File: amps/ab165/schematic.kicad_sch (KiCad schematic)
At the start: 105 parts

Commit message: Fix: schematic sheets — real title block, fitted paper, no lettering through circuitry
Every sheet in the corpus shipped with an EMPTY title block ("Title:" and
"Date:" blank, default "Sheet /" furniture) laid onto a fixed A4/A3 page
regardless of the drawing's size, with prose annotations placed by hand
wherever a coordinate looked free when the amp was first drawn. The result
read as an unfinished alpha under a `verified` badge: KiCanvas's default view
is `zoom_to_page()`, so a 150 x 110 mm circuit on an A3 sheet opened as a
postage stamp, and later edits had pushed live circuitry under the prose.

schematic_lib.py — the builder now records each element as a (kind, points,
extra) tuple instead of a finished string, so `write()` can measure and move
what it emits:

- emits a real `(title_block …)` read from the amp's own meta.yaml — Title =
  designation + style, Date = the verification (or added) date, Rev = the
  verification status, Company = Circuit Codex, plus the licence and source
  URL as comments. Fixes all 34 sheets from one place;
- emits `(paper "User" w h)` cut to the drawing, translated to a fixed margin,
  with the bottom 34 mm strip reserved for the worksheet's title block. Sheet
  utilisation of the drawable area went from as low as ~20% to 92-98%;
- `note()` queues prose into a wrapped band under the circuit, and `caption()`
  places a section heading over the block it names, nudging it clear if it
  would print through anything;
- per-symbol default label offsets (the old single default printed every pot's
  value through its own wiper arrow and every transformer's designator through
  its body), plus `place_labels()`, which moves any designator/value block that
  would print over ink;
- transformers and chokes are drawn, not boxed: iron core between two windings,
  centre taps where the part has them, and an optional `spec` lettering slot for
  a ratio or impedance;
- `gnd()` takes a direction, because a flag defaulting to "down" at the HEAD of
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
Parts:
- V1A, V1B, V2A, V2B, V3B: value 12AX7 -> 12AX7 (7025)
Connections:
- net at CBB.1, CBB2.1, CDEEP.1: no longer RSB.2
- net at CBN.1, CBN2.1: no longer RSN.2
- net at CTN.2: no longer VRTN.1
- net at DBIAS.2 (K): no longer RBIAS.2
- net at CTB.2: no longer VRTB.1
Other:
- note removed: "AB165 — Blackface Bassman-style · Circuit Codex · CC-BY-SA 4.0 · redrawn from circuit facts"
- company: (none) -> Circuit Codex
- title: (none) -> AB165 — Blackface Bassman-style

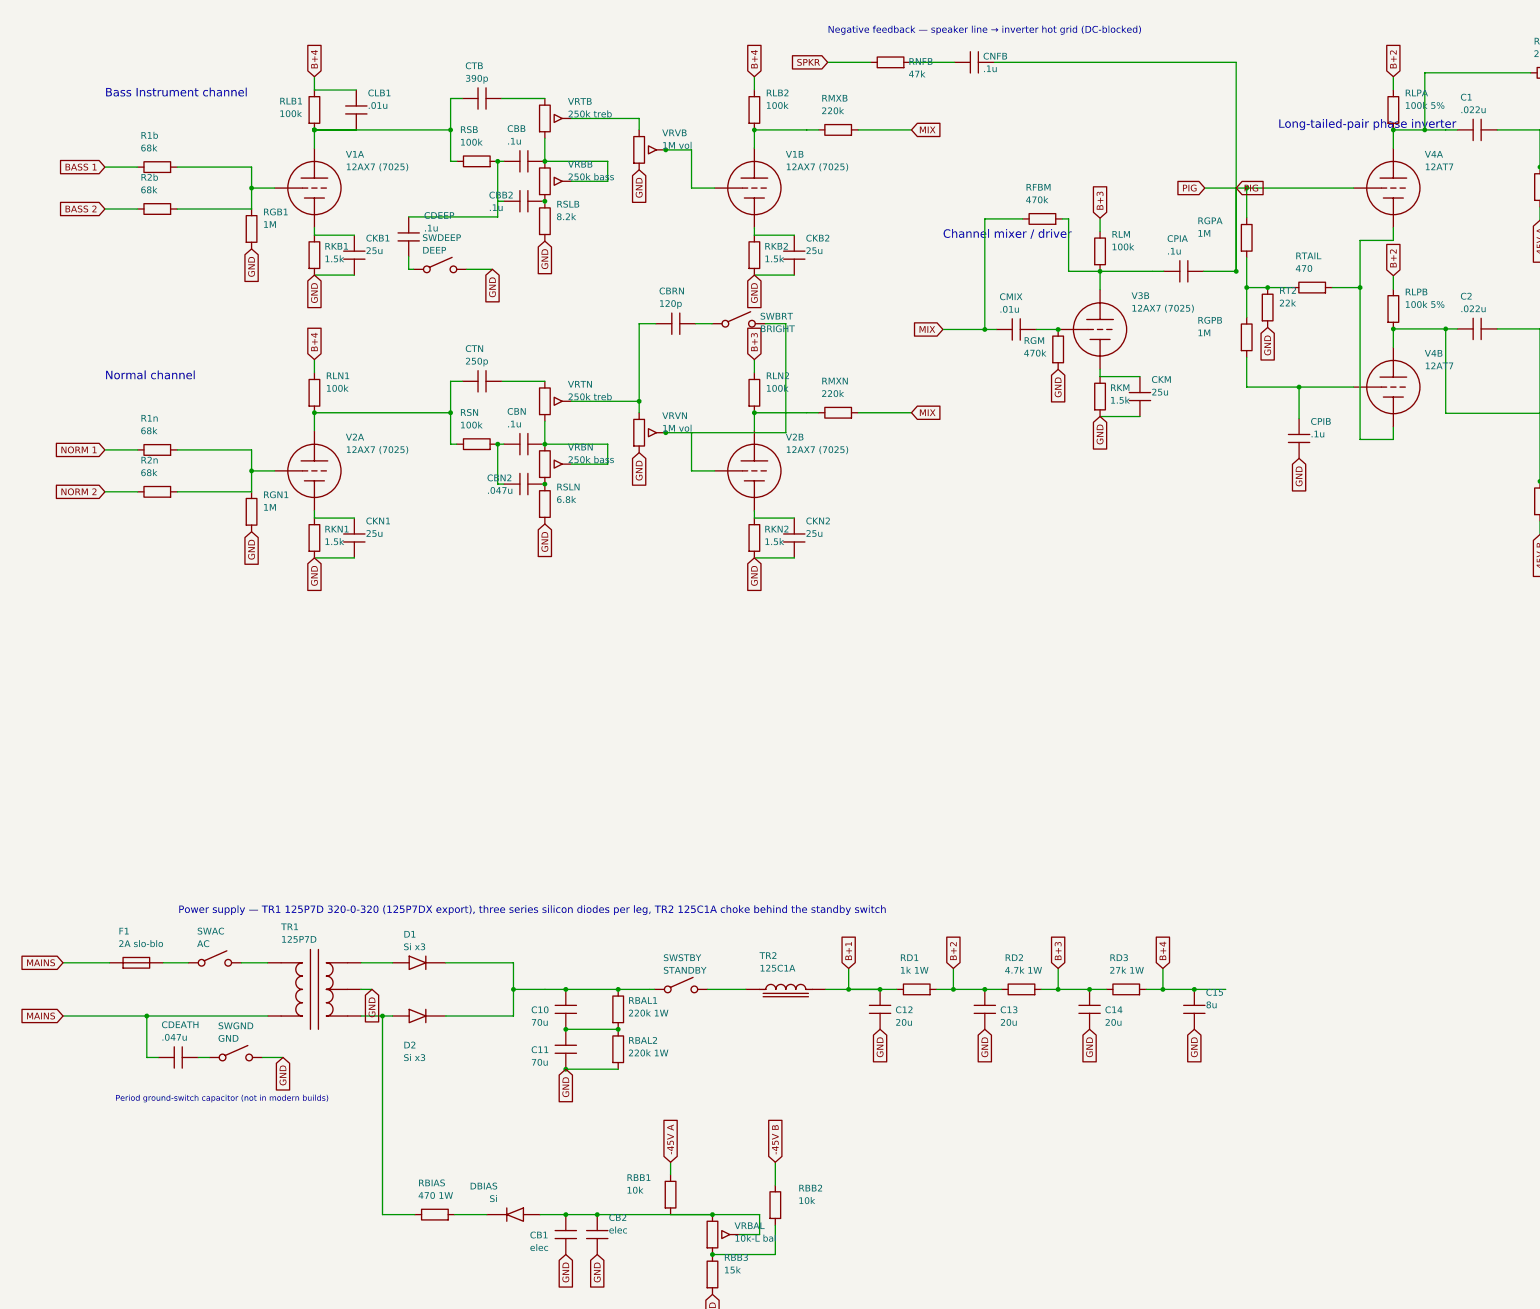
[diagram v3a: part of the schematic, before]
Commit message: Fix: deterministic schematic ids and wires split at every join
- _u() is uuid5 over (amp id, emission order), so a regeneration of an
  unchanged script is byte-identical and a drift gate becomes possible
- write() splits wire segments at symbol pins, wire ends and junction dots,
  so the file connects exactly what the drawing shows under KiCad's
  endpoint-only semantics (270 pins were on a wire's interior; net
  partitions unchanged on all 38 sheets)
- all sheets regenerated; aa864-bassman title block was stale (draft) and
  now matches meta.yaml (verified)

Co-Authored-By: Claude Fable 5.1 <noreply@anthropic.com>
Claude-Session: https://claude.ai/code/session_01KBMfdh37HmCL2iWcBiL5J1
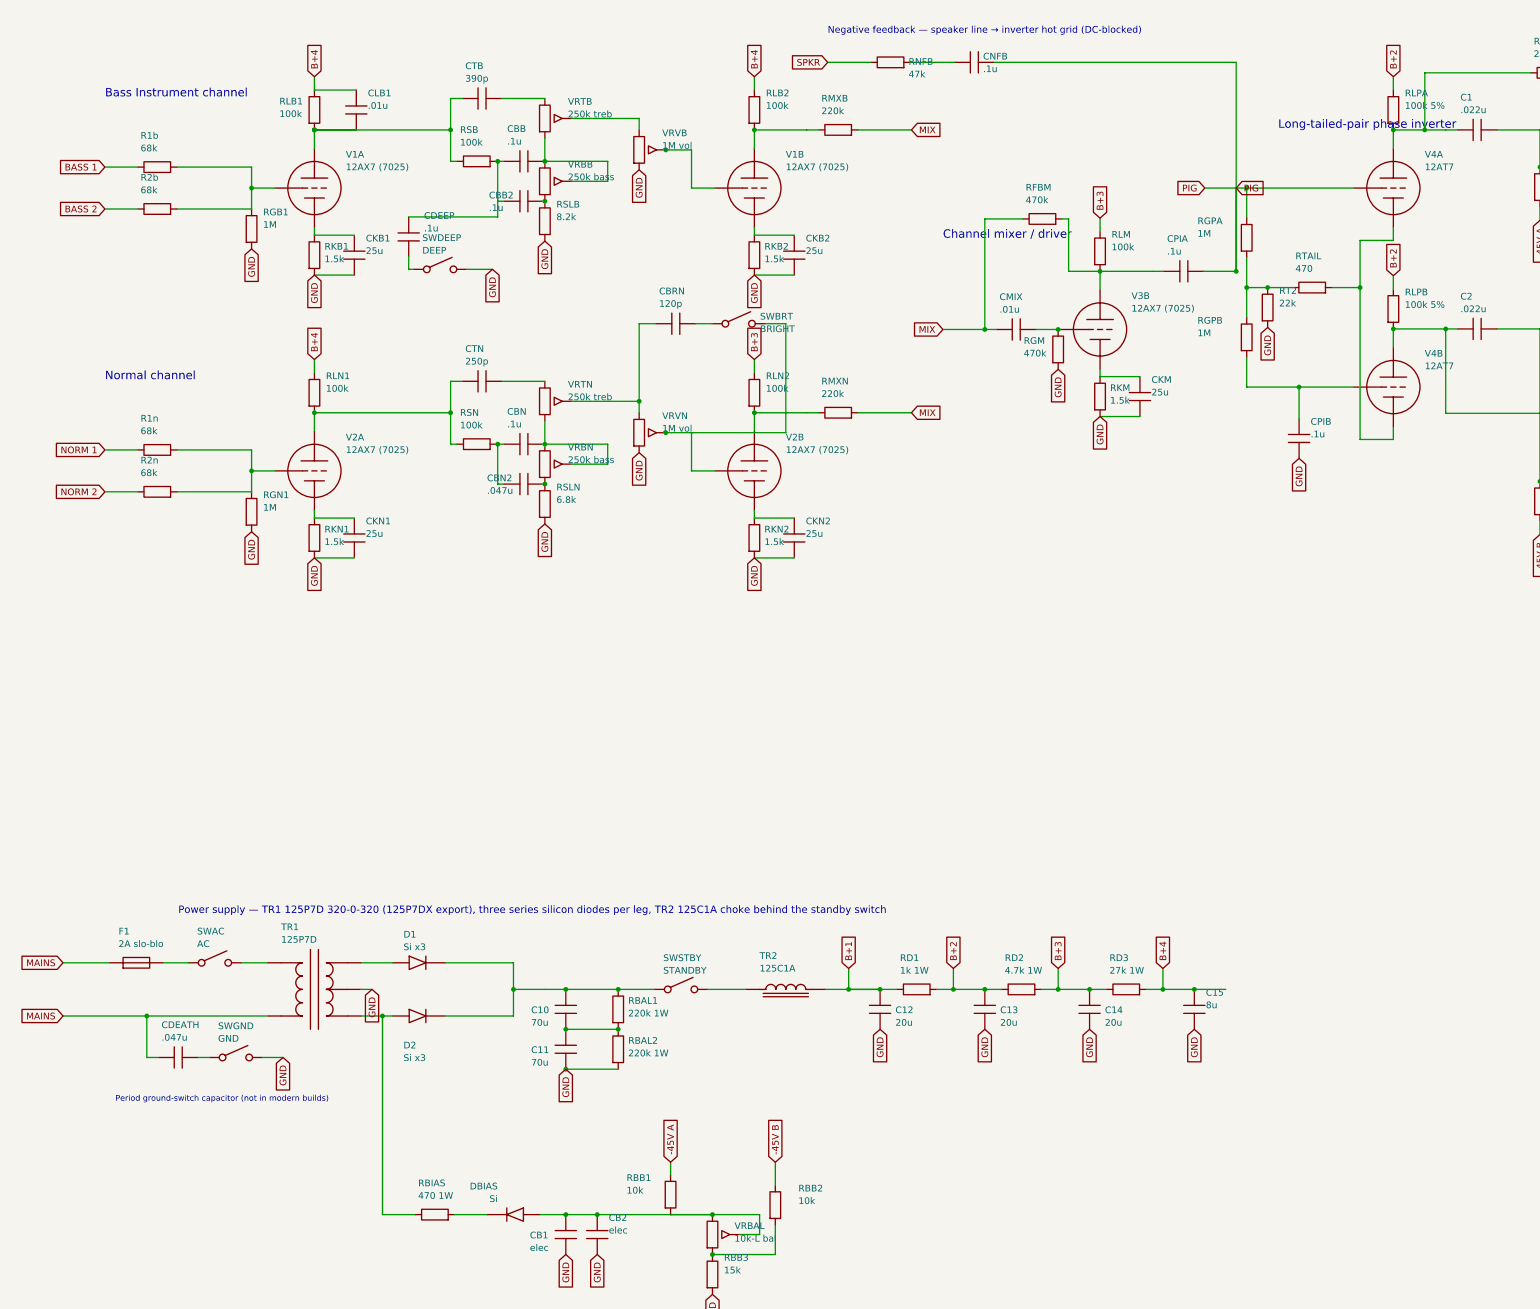
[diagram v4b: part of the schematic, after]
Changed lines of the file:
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@@
   (wire (pts (xy 40.5552 49.82) (xy 54.7452 49.82))
     (stroke (width 0) (type default)))
-  (wire (pts (xy 54.7452 41.82) (xy 54.7452 49.82))
+  (wire (pts (xy 54.7452 41.82) (xy 54.7452 45.82))
+    (stroke (width 0) (type default)))
+  (wire (pts (xy 54.7452 45.82) (xy 54.7452 49.82))
     (stroke (width 0) (type default)))
   (junction (at 54.7452 45.82) (diameter 0) (color 0 0 0 0))
@@
   (global_label "GND" (shape input) (at 66.7452 62.44 270)
     (effects (font (size 1.27 1.27)) (justify right)))
-  (wire (pts (xy 66.7452 34.72) (xy 92.7452 34.72))
+  (wire (pts (xy 66.7452 34.72) (xy 74.7452 34.72))
+    (stroke (width 0) (type default)))
+  (wire (pts (xy 74.7452 34.72) (xy 92.7452 34.72))
     (stroke (width 0) (type default)))
   (junction (at 66.7452 34.72) (diameter 0) (color 0 0 0 0))
@@
   (wire (pts (xy 40.5552 103.82) (xy 54.7452 103.82))
     (stroke (width 0) (type default)))
-  (wire (pts (xy 54.7452 95.82) (xy 54.7452 103.82))
+  (wire (pts (xy 54.7452 95.82) (xy 54.7452 99.82))
+    (stroke (width 0) (type default)))
+  (wire (pts (xy 54.7452 99.82) (xy 54.7452 103.82))
     (stroke (width 0) (type default)))
   (junction (at 54.7452 99.82) (diameter 0) (color 0 0 0 0))
@@
   (wire (pts (xy 196.555 21.82) (xy 242.745 21.82))
     (stroke (width 0) (type default)))
-  (wire (pts (xy 242.745 21.82) (xy 242.745 61.72))
+  (wire (pts (xy 242.745 21.82) (xy 242.745 45.82))
+    (stroke (width 0) (type default)))
+  (wire (pts (xy 242.745 45.82) (xy 242.745 61.72))
     (stroke (width 0) (type default)))
   (text "Long-tailed-pair phase inverter" (at 250.745 33.82 0)
@@
   (global_label "PIG" (shape input) (at 236.745 45.82 180)
     (effects (font (size 1.27 1.27)) (justify right)))
-  (wire (pts (xy 236.745 45.82) (xy 244.745 45.82))
+  (wire (pts (xy 236.745 45.82) (xy 242.745 45.82))
+    (stroke (width 0) (type default)))
+  (wire (pts (xy 242.745 45.82) (xy 244.745 45.82))
     (stroke (width 0) (type default)))
   (junction (at 244.745 45.82) (diameter 0) (color 0 0 0 0))
@@
     (stroke (width 0) (type default)))
   (junction (at 244.745 64.82) (diameter 0) (color 0 0 0 0))
-  (wire (pts (xy 244.745 83.82) (xy 265.125 83.82))
+  (wire (pts (xy 244.745 83.82) (xy 254.745 83.82))
+    (stroke (width 0) (type default)))
+  (wire (pts (xy 254.745 83.82) (xy 265.125 83.82))
     (stroke (width 0) (type default)))
   (junction (at 254.745 83.82) (diameter 0) (color 0 0 0 0))
@@
   (wire (pts (xy 272.745 93.82) (xy 266.395 93.82))
     (stroke (width 0) (type default)))
-  (wire (pts (xy 266.395 55.82) (xy 266.395 93.82))
+  (wire (pts (xy 266.395 55.82) (xy 266.395 64.82))
+    (stroke (width 0) (type default)))
+  (wire (pts (xy 266.395 64.82) (xy 266.395 93.82))
     (stroke (width 0) (type default)))
   (junction (at 266.395 64.82) (diameter 0) (color 0 0 0 0))
@@
     (effects (font (size 1.6 1.6)) (justify left)))
   (junction (at 272.745 34.72) (diameter 0) (color 0 0 0 0))
-  (wire (pts (xy 272.745 34.72) (xy 282.745 34.72))
+  (wire (pts (xy 272.745 34.72) (xy 278.745 34.72))
+    (stroke (width 0) (type default)))
+  (wire (pts (xy 278.745 34.72) (xy 282.745 34.72))
     (stroke (width 0) (type default)))
   (symbol (lib_id "cx:C") (at 288.745 34.72 90) (unit 1)
@@
   (global_label "MAINS" (shape input) (at 18.7452 203.9 180)
     (effects (font (size 1.27 1.27)) (justify right)))
-  (wire (pts (xy 18.7452 203.9) (xy 57.8552 203.9))
+  (wire (pts (xy 18.7452 203.9) (xy 34.7452 203.9))
+    (stroke (width 0) (type default)))
+  (wire (pts (xy 34.7452 203.9) (xy 57.8552 203.9))
     (stroke (width 0) (type default)))
   (junction (at 34.7452 203.9) (diameter 0) (color 0 0 0 0))
@@
   (wire (pts (xy 91.8252 193.74) (xy 104.745 193.74))
     (stroke (width 0) (type default)))
-  (wire (pts (xy 75.6352 203.9) (xy 81.6652 203.9))
+  (wire (pts (xy 75.6352 203.9) (xy 79.7452 203.9))
+    (stroke (width 0) (type default)))
+  (wire (pts (xy 79.7452 203.9) (xy 81.6652 203.9))
     (stroke (width 0) (type default)))
   (symbol (lib_id "cx:DIODE_SS") (at 86.7452 203.9 0) (unit 1)
@@
   (wire (pts (xy 91.8252 203.9) (xy 104.745 203.9))
     (stroke (width 0) (type default)))
-  (wire (pts (xy 104.745 193.74) (xy 104.745 203.9))
+  (wire (pts (xy 104.745 193.74) (xy 104.745 198.82))
+    (stroke (width 0) (type default)))
+  (wire (pts (xy 104.745 198.82) (xy 104.745 203.9))
     (stroke (width 0) (type default)))
   (junction (at 104.745 198.82) (diameter 0) (color 0 0 0 0))
@@
   (wire (pts (xy 104.745 198.82) (xy 110.745 198.82))
     (stroke (width 0) (type default)))
-  (wire (pts (xy 110.745 198.82) (xy 130.745 198.82))
+  (wire (pts (xy 110.745 198.82) (xy 114.745 198.82))
+    (stroke (width 0) (type default)))
+  (wire (pts (xy 114.745 198.82) (xy 124.745 198.82))
+    (stroke (width 0) (type default)))
+  (wire (pts (xy 124.745 198.82) (xy 130.745 198.82))
     (stroke (width 0) (type default)))
   (junction (at 114.745 198.82) (diameter 0) (color 0 0 0 0))
@@
   (wire (pts (xy 141.825 198.82) (xy 149.125 198.82))
     (stroke (width 0) (type default)))
-  (wire (pts (xy 164.365 198.82) (xy 174.745 198.82))
+  (wire (pts (xy 164.365 198.82) (xy 168.745 198.82))
+    (stroke (width 0) (type default)))
+  (wire (pts (xy 168.745 198.82) (xy 174.745 198.82))
     (stroke (width 0) (type default)))
   (junction (at 168.745 198.82) (diameter 0) (color 0 0 0 0))
@@
   (wire (pts (xy 93.5552 241.82) (xy 99.6652 241.82))
     (stroke (width 0) (type default)))
-  (wire (pts (xy 109.825 241.82) (xy 124.745 241.82))
+  (wire (pts (xy 109.825 241.82) (xy 114.745 241.82))
+    (stroke (width 0) (type default)))
+  (wire (pts (xy 114.745 241.82) (xy 120.745 241.82))
+    (stroke (width 0) (type default)))
+  (wire (pts (xy 120.745 241.82) (xy 124.745 241.82))
     (stroke (width 0) (type default)))
   (junction (at 114.745 241.82) (diameter 0) (color 0 0 0 0))
@@
   (global_label "GND" (shape input) (at 120.745 249.44 270)
     (effects (font (size 1.27 1.27)) (justify right)))
-  (wire (pts (xy 124.745 241.82) (xy 142.745 241.82))
+  (wire (pts (xy 124.745 241.82) (xy 134.745 241.82))
+    (stroke (width 0) (type default)))
+  (wire (pts (xy 134.745 241.82) (xy 142.745 241.82))
     (stroke (width 0) (type default)))
   (symbol (lib_id "cx:POT") (at 142.745 245.63 0) (unit 1)

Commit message: Add: real tube pin numbers and readable valve glyphs on every schematic
Phase B of the drawing program. A factory service sheet numbers every tube
pin, because the number is what a technician puts a probe on. This corpus
printed none, and the numbers hidden in its symbols were positional
placeholders (P=1, G=2, K=3) that would have published a 6V6GT's plate as
pin 1 when it is pin 3.

1055 electrodes now carry the real number, 1027 lettered (27 are shared
filaments deduped, 1 dropped for want of clear space on the 6G2). Resolved per
instance from reference/tubes/<slug>.yaml through the same alias resolution the
layout renderer uses, so a 12AX7 section and a 6SL7 section each get their own
basing. A valve whose basing the corpus does not carry prints nothing rather
than a wrong number.

Section letters and basing units are now separate things, which cost a detour
worth recording. The RCA 12AX7-A sheet reads "Pin 1 - Plate of Unit No.2 ...
Pin 6 - Plate of Unit No.1", so unit numbering is not pin order; the 5Y3 and
GZ34 number their units in opposite pin order, so nothing positional can
express it. But the section LETTER is a designator, not a basing fact: this
corpus, like every technician, calls the first stage in signal order V1A, and
five amps' prose already did. On four amps the factory sheets put that first
stage on the other half -- the AA764's own schematic prints +200 V on pin 1 --
so those drawings now state their unit explicitly, each citing its source, and
no letter, netlist, parts list or layout comment changed. 183 layout comments
agree with the printed numbers, 0 disagree. A guard fires if two halves of one
bottle resolve to the same unit, which is exactly how this was found.

Glyphs: the cathode gains a bracket and filament hairpin so it can no longer be
confused with the plate bar, the pentode's screen sits on its own row, and a
rectifier draws as one envelope over its sections instead of two apparent
bottles. Line weights are scaled per sheet to a co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
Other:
- note added: "1"
- note added: "2"
- note added: "3"
- note added: "4"
- note added: "5"
- note added: "6"
- note added: "7"
- note added: "8"

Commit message: Fix: schematic sheet notes no longer name repository files
Thirty-seven committed sheets rendered footnotes and section notes such as
"Heaters and PT primary omitted — see netlist.cir and meta.yaml" or
"excluded from netlist.cir (notes.md)" to visitors through KiCanvas. The
prose sweeps never counted sheets. Rewritten in the site's own words — the
netlist, the sources list, the circuit story, the parts list, the board
drawing — in 59 strings across 33 draw scripts, keeping every technical
claim as it was; the three tone sheets (6G4, 6G5, 6G6-B) are under repair
elsewhere and keep theirs for now. The sweep touched only strings passed to
the sheet's note, text, caption and footnote calls, never a path or a value.

Gates: check_schematics 40/0, connectivity 0 isolated pins;
verify_schematic_nets 40 clean; only the regenerated sheets and their served
copies changed.

Co-Authored-By: Claude Fable 5.1 <noreply@anthropic.com>
Claude-Session: https://claude.ai/code/session_01KBMfdh37HmCL2iWcBiL5J1
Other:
- note added: "Heaters, pilot lamp and the PT primary beyond the drawn switch/fuse are omitted here — see the netlist, the sources list and the board drawing. Rails: B+1 +425 · B+2 +415 · B+3 +390 · B+4 +320 · bias -45 V"
- note removed: "Heaters, pilot lamp and the PT primary beyond the drawn switch/fuse are omitted here — see netlist.cir, meta.yaml, layout.yaml. Rails: B+1 +425 · B+2 +415 · B+3 +390 · B+4 +320 · bias -45 V"
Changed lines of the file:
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@@
   (text "8" (at 335.595 107.535 0)
     (effects (font (size 1.1 1.1)) (justify left)))
-  (text "Heaters, pilot lamp and the PT primary beyond the drawn switch/fuse are omitted here — see netlist.cir, meta.yaml, layout.yaml. Rails: B+1 +425 · B+2 +415 · B+3 +390 · B+4 +320 · bias -45 V" (at 12.7 268.218 0)
+  (text "Heaters, pilot lamp and the PT primary beyond the drawn switch/fuse are omitted here — see the netlist, the sources list and the board drawing. Rails: B+1 +425 · B+2 +415 · B+3 +390 · B+4 +320 · bias -45 V" (at 12.7 268.218 0)
     (effects (font (size 1.2 1.2)) (justify left)))
   (text "Bias supply — one HT leg through 470 Ω · 1 W and a silicon diode; the 10 kΩ-L balance control gives each output tube its own 10 kΩ leg" (at 12.7 272.618 0)
